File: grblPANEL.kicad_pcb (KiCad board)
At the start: 4 copper layers, 0 parts

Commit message: PCB layout - WIP
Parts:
- added C101: 470n, Capacitor_SMD:C_0805_2012Metric, F.Cu at (96.0, 131.0)
- added C102: 10u, Capacitor_SMD:C_1206_3216Metric, F.Cu at (92.0, 133.0)
- added C103: 1u, Capacitor_SMD:C_0603_1608Metric, F.Cu at (80.5, 129.0)
- added C104: 1u, Capacitor_SMD:C_0603_1608Metric, F.Cu at (78.5, 129.0)
- added C105: 10u, Capacitor_SMD:C_1206_3216Metric, F.Cu at (72.0, 129.0)
- added C106: 22u, Capacitor_SMD:C_1206_3216Metric, F.Cu at (57.5, 129.0)
- added C201: 4u7, Capacitor_SMD:C_0805_2012Metric, F.Cu at (33.5, 98.5)
- added C202: 100n, Capacitor_SMD:C_0603_1608Metric, F.Cu at (35.5, 102.0)
- added C203: 100n, Capacitor_SMD:C_0603_1608Metric, F.Cu at (35.5, 98.5)
- added C204: 100n, Capacitor_SMD:C_0603_1608Metric, F.Cu at (49.5, 102.0)
- added C205: 100n, Capacitor_SMD:C_0603_1608Metric, F.Cu at (72.0, 75.5)
- added C206: 10p, Capacitor_SMD:C_0603_1608Metric, F.Cu at (29.5, 105.5)
- added C207: 10p, Capacitor_SMD:C_0603_1608Metric, F.Cu at (35.5, 105.5)
- added C208: 100n, Capacitor_SMD:C_0603_1608Metric, F.Cu at (51.0, 97.0)
- added C301: 100n, Capacitor_SMD:C_0603_1608Metric, F.Cu at (88.5, 144.0)
- added C302: 10p, Capacitor_SMD:C_0603_1608Metric, F.Cu at (100.5, 141.0)
- added C303: 10p, Capacitor_SMD:C_0603_1608Metric, F.Cu at (100.5, 147.0)
- added C401: 100n, Capacitor_SMD:C_0603_1608Metric, F.Cu at (98.0, 157.0)
- added C501: 4u7, Capacitor_SMD:C_0805_2012Metric, F.Cu at (-30.8, 109.7)
- added C502: 100n, Capacitor_SMD:C_0603_1608Metric, F.Cu at (-42.0, 122.4)
- added C503: 100n, Capacitor_SMD:C_0603_1608Metric, F.Cu at (-50.0, 122.4)
- added C601: 10u, Capacitor_SMD:C_1206_3216Metric, F.Cu at (-69.7, 15.5)
- added C602: 100n, Capacitor_SMD:C_0603_1608Metric, F.Cu at (-76.1, 50.2)
- added D101: SMAJ24CA, Diode_SMD:D_SMA, F.Cu at (103.0, 129.0)
- added D102: D_Schottky, Diode_SMD:D_SOD-323, F.Cu at (87.5, 134.5)
- added D103: LED, LED_SMD:LED_0603_1608Metric, F.Cu at (49.0, 129.0)
- added D201: LED, LED_SMD:LED_0603_1608Metric, F.Cu at (47.0, 111.0)
- added D202: D_TVS, Diode_SMD:D_SOD-323, F.Cu at (49.5, 79.0)
- added D203: D_TVS, Diode_SMD:D_SOD-323, F.Cu at (52.0, 91.0)
- added D204: D_TVS, Diode_SMD:D_SOD-323, F.Cu at (48.0, 91.0)
- added D205: D_TVS, Diode_SMD:D_SOD-323, F.Cu at (44.0, 91.0)
- added D301: CDSOT23-SM712, Package_TO_SOT_SMD:SOT-23, F.Cu at (103.5, 144.0)
- added D401: CDSOT23-SM712, Package_TO_SOT_SMD:SOT-23, F.Cu at (104.0, 160.0)
- added D601: D_TVS, Diode_SMD:D_SOD-323, F.Cu at (-22.0, 52.0)
- added D602: D_TVS, Diode_SMD:D_SOD-323, F.Cu at (-22.0, 50.0)
- added D603: D_TVS, Diode_SMD:D_SOD-323, F.Cu at (-22.0, 48.0)
- added D604: D_TVS, Diode_SMD:D_SOD-323, F.Cu at (-22.0, 46.0)
- added D605: D_TVS, Diode_SMD:D_SOD-323, F.Cu at (-22.0, 44.0)
- added D606: D_TVS, Diode_SMD:D_SOD-323, F.Cu at (-22.0, 42.0)
- added D607: D_TVS, Diode_SMD:D_SOD-323, F.Cu at (-22.0, 40.0)
- added D608: D_TVS, Diode_SMD:D_SOD-323, F.Cu at (-22.0, 38.0)
- added D609: D_TVS, Diode_SMD:D_SOD-323, F.Cu at (-22.0, 36.0)
- added D610: D_TVS, Diode_SMD:D_SOD-323, F.Cu at (-22.0, 34.0)
- added D611: D_TVS, Diode_SMD:D_SOD-323, F.Cu at (-22.0, 32.0)
- added D612: D_TVS, Diode_SMD:D_SOD-323, F.Cu at (-22.1, 30.0)
- added D613: D_TVS, Diode_SMD:D_SOD-323, F.Cu at (-22.0, 28.0)
- added D614: D_TVS, Diode_SMD:D_SOD-323, F.Cu at (-22.0, 26.0)
- added D615: D_TVS, Diode_SMD:D_SOD-323, F.Cu at (-22.0, 24.0)
- added D616: D_TVS, Diode_SMD:D_SOD-323, F.Cu at (-22.0, 22.0)
- added D617: D_TVS, Diode_SMD:D_SOD-323, F.Cu at (-22.0, 20.0)
- added D618: D_TVS, Diode_SMD:D_SOD-323, F.Cu at (-22.0, 18.0)
- added D619: D_TVS, Diode_SMD:D_SOD-323, F.Cu at (-22.0, 16.0)
- added D701: D_TVS, Diode_SMD:D_SOD-323, F.Cu at (82.0, 176.0)
- added D702: D_TVS, Diode_SMD:D_SOD-323, F.Cu at (66.0, 176.0)
- added D703: D_TVS, Diode_SMD:D_SOD-323, F.Cu at (78.0, 176.0)
- added D704: D_TVS, Diode_SMD:D_SOD-323, F.Cu at (62.0, 176.0)
- added D705: D_TVS, Diode_SMD:D_SOD-323, F.Cu at (50.0, 176.0)
- added D706: D_TVS, Diode_SMD:D_SOD-323, F.Cu at (34.0, 176.0)
- added D707: D_TVS, Diode_SMD:D_SOD-323, F.Cu at (46.0, 176.0)
- added D708: D_TVS, Diode_SMD:D_SOD-323, F.Cu at (30.0, 176.0)
- added J101: Conn_01x02, TerminalBlock_Phoenix:TerminalBlock_Phoenix_PT-1,5-2-3.5-H_1x02_P3.50mm_Horizontal, B.Cu at (107.5, 127.2)
- added J201: 2x5x1.27mm, dresco:FTSH-105-01-L-DV-K, F.Cu at (48.0, 85.0)
- added J202: USB_C_Receptacle_USB2.0, Connector_USB:USB_C_Receptacle_HRO_TYPE-C-31-M-12, F.Cu at (64.0, 97.0)
- added J301: Conn_01x02, TerminalBlock_Phoenix:TerminalBlock_Phoenix_PT-1,5-2-3.5-H_1x02_P3.50mm_Horizontal, B.Cu at (107.5, 142.2)
- added J401: Conn_01x02, TerminalBlock_Phoenix:TerminalBlock_Phoenix_PT-1,5-2-3.5-H_1x02_P3.50mm_Horizontal, B.Cu at (107.5, 158.2)
- added J501: ILI9488, Connector_FFC-FPC:Hirose_FH12-40S-0.5SH_1x40-1MP_P0.50mm_Horizontal, F.Cu at (-46.6, 111.7)
- added J601: Conn_02x10_Odd_Even, Connector_IDC:IDC-Header_2x10_P2.54mm_Vertical, F.Cu at (-9.75, 23.1)
- added J701: Conn_01x04, TerminalBlock_Phoenix:TerminalBlock_Phoenix_PT-1,5-4-3.5-H_1x04_P3.50mm_Horizontal, B.Cu at (82.0, 179.0)
- added J702: Conn_01x04, TerminalBlock_Phoenix:TerminalBlock_Phoenix_PT-1,5-4-3.5-H_1x04_P3.50mm_Horizontal, B.Cu at (66.0, 179.0)
- added J703: Conn_01x04, TerminalBlock_Phoenix:TerminalBlock_Phoenix_PT-1,5-4-3.5-H_1x04_P3.50mm_Horizontal, B.Cu at (50.0, 179.0)
- added J704: Conn_01x04, TerminalBlock_Phoenix:TerminalBlock_Phoenix_PT-1,5-4-3.5-H_1x04_P3.50mm_Horizontal, B.Cu at (34.0, 179.0)
- added JP301: Jumper_2_Bridged, Connector_PinHeader_2.54mm:PinHeader_1x02_P2.54mm_Vertical, B.Cu at (98.2, 144.0)
- added JP401: Jumper_2_Bridged, Connector_PinHeader_2.54mm:PinHeader_1x02_P2.54mm_Vertical, B.Cu at (98.2, 160.0)
- added L101: 10n, Inductor_SMD:L_0603_1608Metric, F.Cu at (79.5, 132.0)
- added Q501: Q_NPN_BEC - S8050, Package_TO_SOT_SMD:SOT-23, F.Cu at (-57.7, 119.4)
- added R101: 2m2, Resistor_SMD:R_0603_1608Metric, F.Cu at (98.0, 131.0)
- added R102: 1m1, Resistor_SMD:R_0603_1608Metric, F.Cu at (98.0, 127.0)
- added R103: 2m2, Resistor_SMD:R_0603_1608Metric, F.Cu at (100.0, 131.0)
- added R104: 249k, Resistor_SMD:R_0603_1608Metric, F.Cu at (100.0, 127.0)
- added R105: 150k, Resistor_SMD:R_0603_1608Metric, F.Cu at (96.0, 127.0)
- added R106: 1k5, Resistor_SMD:R_0603_1608Metric, F.Cu at (87.5, 128.0)
- added R107: DNP, Resistor_SMD:R_0603_1608Metric, F.Cu at (87.5, 132.0)
- added R108: 0, Resistor_SMD:R_0603_1608Metric, F.Cu at (87.5, 130.0)
- added R109: 1k, Resistor_SMD:R_0603_1608Metric, F.Cu at (46.5, 129.0)
- added R201: 0, Resistor_SMD:R_0603_1608Metric, F.Cu at (33.5, 102.0)
- added R202: 200, Resistor_SMD:R_0603_1608Metric, F.Cu at (59.0, 75.5)
- added R203: 0, Resistor_SMD:R_0603_1608Metric, F.Cu at (52.0, 103.0)
- added R204: 0, Resistor_SMD:R_0603_1608Metric, F.Cu at (52.0, 101.0)
- added R205: 1k, Resistor_SMD:R_0603_1608Metric, F.Cu at (43.8, 111.0)
- added R206: 0, Resistor_SMD:R_0603_1608Metric, F.Cu at (32.5, 108.5)
- added R207: 5k1, Resistor_SMD:R_0603_1608Metric, F.Cu at (56.5, 100.8)
- added R208: 5k1, Resistor_SMD:R_0603_1608Metric, F.Cu at (56.5, 93.0)
- added R209: 49R9, Resistor_SMD:R_0603_1608Metric, F.Cu at (52.0, 93.0)
- added R210: 49R9, Resistor_SMD:R_0603_1608Metric, F.Cu at (48.0, 93.0)
- added R211: 49R9, Resistor_SMD:R_0603_1608Metric, F.Cu at (44.0, 93.0)
- added R301: DNP, Resistor_SMD:R_0603_1608Metric, F.Cu at (98.5, 147.0)
- added R302: 10k, Resistor_SMD:R_0603_1608Metric, F.Cu at (95.5, 140.0)
- added R303: 120, Resistor_SMD:R_0603_1608Metric, F.Cu at (98.5, 141.0)
- added R401: 10k, Resistor_SMD:R_0603_1608Metric, F.Cu at (87.0, 161.0)
- added R402: 10k, Resistor_SMD:R_0603_1608Metric, F.Cu at (87.0, 159.0)
- added R403: 120, Resistor_SMD:R_0603_1608Metric, F.Cu at (98.0, 163.0)
- added R404: DNP, Resistor_SMD:R_0603_1608Metric, F.Cu at (100.0, 163.0)
- added R405: DNP, Resistor_SMD:R_0603_1608Metric, F.Cu at (100.0, 157.0)
- added R406: 10, Resistor_SMD:R_1206_3216Metric, F.Cu at (103.5, 163.5)
- added R407: 10, Resistor_SMD:R_1206_3216Metric, F.Cu at (103.5, 156.5)
- added R501: 1k, Resistor_SMD:R_0603_1608Metric, F.Cu at (-37.1, 118.4)
- added R502: 10k, Resistor_SMD:R_0603_1608Metric, F.Cu at (-50.0, 125.0)
- added R503: 5R6, Resistor_SMD:R_0603_1608Metric, F.Cu at (-46.0, 122.4)
- added R504: 0, Resistor_SMD:R_0603_1608Metric, F.Cu at (-46.0, 125.0)
- added R505: 1k, Resistor_SMD:R_0603_1608Metric, F.Cu at (-31.0, 116.5)
- added R601: 10k, Resistor_SMD:R_0603_1608Metric, F.Cu at (-89.0, 47.0)
- added R602: 10k, Resistor_SMD:R_0603_1608Metric, F.Cu at (-61.8, 53.0)
- added R603: 10k, Resistor_SMD:R_0603_1608Metric, F.Cu at (-61.8, 55.0)
- added R604: 10k, Resistor_SMD:R_0603_1608Metric, F.Cu at (-61.8, 57.0)
- added R605: 200, Resistor_SMD:R_0603_1608Metric, F.Cu at (-29.5, 16.0)
- added R606: 200, Resistor_SMD:R_0603_1608Metric, F.Cu at (-29.5, 18.0)
- added R607: 200, Resistor_SMD:R_0603_1608Metric, F.Cu at (-29.5, 20.0)
- added R608: 200, Resistor_SMD:R_0603_1608Metric, F.Cu at (-29.5, 22.0)
- added R609: 200, Resistor_SMD:R_0603_1608Metric, F.Cu at (-29.5, 24.0)
- added R610: 200, Resistor_SMD:R_0603_1608Metric, F.Cu at (-29.5, 26.0)
- added R611: 200, Resistor_SMD:R_0603_1608Metric, F.Cu at (-29.5, 28.0)
- added R612: 200, Resistor_SMD:R_0603_1608Metric, F.Cu at (-29.5, 30.0)
- added R613: 200, Resistor_SMD:R_0603_1608Metric, F.Cu at (-29.5, 32.0)
- added R614: 200, Resistor_SMD:R_0603_1608Metric, F.Cu at (-29.5, 34.0)
- added R615: 200, Resistor_SMD:R_0603_1608Metric, F.Cu at (-29.5, 36.0)
- added R616: 200, Resistor_SMD:R_0603_1608Metric, F.Cu at (-29.5, 38.0)
- added R617: 200, Resistor_SMD:R_0603_1608Metric, F.Cu at (-29.5, 40.0)
- added R618: 200, Resistor_SMD:R_0603_1608Metric, F.Cu at (-29.5, 42.0)
- added R619: 200, Resistor_SMD:R_0603_1608Metric, F.Cu at (-29.5, 44.0)
- added R620: 200, Resistor_SMD:R_0603_1608Metric, F.Cu at (-29.5, 46.0)
- added R621: 200, Resistor_SMD:R_0603_1608Metric, F.Cu at (-29.5, 48.0)
- added R622: 200, Resistor_SMD:R_0603_1608Metric, F.Cu at (-29.5, 50.0)
- added R623: 200, Resistor_SMD:R_0603_1608Metric, F.Cu at (-29.5, 52.0)
- added R701: 200, Resistor_SMD:R_0603_1608Metric, F.Cu at (82.0, 174.0)
- added R702: 200, Resistor_SMD:R_0603_1608Metric, F.Cu at (78.0, 174.0)
- added R703: 200, Resistor_SMD:R_0603_1608Metric, F.Cu at (66.0, 174.0)
- added R704: 200, Resistor_SMD:R_0603_1608Metric, F.Cu at (62.0, 174.0)
- added R705: 200, Resistor_SMD:R_0603_1608Metric, F.Cu at (50.0, 174.0)
- added R706: 200, Resistor_SMD:R_0603_1608Metric, F.Cu at (46.0, 174.0)
- added R707: 200, Resistor_SMD:R_0603_1608Metric, F.Cu at (34.0, 174.0)
- added R708: 200, Resistor_SMD:R_0603_1608Metric, F.Cu at (30.0, 174.0)
- added SW201: SW_Push, Button_Switch_SMD:SW_Push_1P1T_NO_6x6mm_H9.5mm, F.Cu at (59.0, 69.5)
- added SW202: SW_Push, Button_Switch_SMD:SW_Push_1P1T_NO_6x6mm_H9.5mm, F.Cu at (72.0, 69.5)
- added TP101: TestPoint, TestPoint:TestPoint_THTPad_D2.0mm_Drill1.0mm, F.Cu at (103.0, 122.0)
- added TP102: TestPoint, TestPoint:TestPoint_THTPad_D2.0mm_Drill1.0mm, F.Cu at (94.0, 122.0)
- added TP103: TestPoint, TestPoint:TestPoint_THTPad_D2.0mm_Drill1.0mm, F.Cu at (90.0, 122.0)
- added TP104: TestPoint, TestPoint:TestPoint_THTPad_D2.0mm_Drill1.0mm, F.Cu at (103.0, 135.0)
- added TP105: TestPoint, TestPoint:TestPoint_THTPad_D2.0mm_Drill1.0mm, F.Cu at (65.0, 122.0)
- added TP301: TestPoint, TestPoint:TestPoint_THTPad_D2.0mm_Drill1.0mm, F.Cu at (88.5, 140.0)
- added TP302: TestPoint, TestPoint:TestPoint_THTPad_D2.0mm_Drill1.0mm, F.Cu at (88.5, 148.0)
- added TP303: TestPoint, TestPoint:TestPoint_THTPad_D2.0mm_Drill1.0mm, F.Cu at (103.0, 139.5)
- added TP304: TestPoint, TestPoint:TestPoint_THTPad_D2.0mm_Drill1.0mm, F.Cu at (103.0, 148.5)
- added TP401: TestPoint, TestPoint:TestPoint_THTPad_D2.0mm_Drill1.0mm, F.Cu at (88.5, 155.0)
- added TP402: TestPoint, TestPoint:TestPoint_THTPad_D2.0mm_Drill1.0mm, F.Cu at (88.5, 165.0)
- added TP403: TestPoint, TestPoint:TestPoint_THTPad_D2.0mm_Drill1.0mm, F.Cu at (98.5, 153.0)
- added TP404: TestPoint, TestPoint:TestPoint_THTPad_D2.0mm_Drill1.0mm, F.Cu at (102.5, 153.0)
- added TP501: TestPoint, TestPoint:TestPoint_THTPad_D2.0mm_Drill1.0mm, F.Cu at (-58.1, 123.6)
- added TP502: TestPoint, TestPoint:TestPoint_THTPad_D2.0mm_Drill1.0mm, F.Cu at (-45.1, 119.2)
- added TP503: TestPoint, TestPoint:TestPoint_THTPad_D2.0mm_Drill1.0mm, F.Cu at (-31.0, 113.2)
- added TP504: TestPoint, TestPoint:TestPoint_THTPad_D2.0mm_Drill1.0mm, F.Cu at (-53.2, 119.2)
- added TP505: TestPoint, TestPoint:TestPoint_THTPad_D2.0mm_Drill1.0mm, F.Cu at (-54.1, 123.6)
- added TP506: TestPoint, TestPoint:TestPoint_THTPad_D2.0mm_Drill1.0mm, F.Cu at (-49.2, 119.2)
- added TP507: TestPoint, TestPoint:TestPoint_THTPad_D2.0mm_Drill1.0mm, F.Cu at (-41.1, 119.2)
- added TP601: TestPoint, TestPoint:TestPoint_THTPad_D2.0mm_Drill1.0mm, F.Cu at (-58.0, 24.7)
- added TP602: TestPoint, TestPoint:TestPoint_THTPad_D2.0mm_Drill1.0mm, F.Cu at (-62.0, 24.7)
- added TP701: TestPoint, TestPoint:TestPoint_THTPad_D2.0mm_Drill1.0mm, F.Cu at (82.0, 170.0)
- added TP702: TestPoint, TestPoint:TestPoint_THTPad_D2.0mm_Drill1.0mm, F.Cu at (66.0, 170.0)
- added TP703: TestPoint, TestPoint:TestPoint_THTPad_D2.0mm_Drill1.0mm, F.Cu at (78.5, 170.0)
- added TP704: TestPoint, TestPoint:TestPoint_THTPad_D2.0mm_Drill1.0mm, F.Cu at (62.5, 170.0)
- added TP705: TestPoint, TestPoint:TestPoint_THTPad_D2.0mm_Drill1.0mm, F.Cu at (50.0, 170.0)
- added TP706: TestPoint, TestPoint:TestPoint_THTPad_D2.0mm_Drill1.0mm, F.Cu at (34.0, 170.0)
- added TP707: TestPoint, TestPoint:TestPoint_THTPad_D2.0mm_Drill1.0mm, F.Cu at (46.5, 170.0)
- added TP708: TestPoint, TestPoint:TestPoint_THTPad_D2.0mm_Drill1.0mm, F.Cu at (30.5, 170.0)
- added U101: MAX17612A, dresco:TDFN-10-1EP_3x3mm_P0.5mm_EP1.6x2.39mm_ThermalVias, F.Cu at (92.0, 129.0)
- added U102: AZ1117-3.3, Package_TO_SOT_SMD:SOT-223-3_TabPin2, F.Cu at (65.0, 129.0)
- added U201: STM32G0B1CxTxN, Package_QFP:LQFP-48_7x7mm_P0.5mm, F.Cu at (42.5, 102.0)
- added U202: USBLC6-2SC6, Package_TO_SOT_SMD:SOT-23-6, F.Cu at (55.0, 97.0)
- added U301: SN65HVD230, Package_SO:SOIC-8_3.9x4.9mm_P1.27mm, F.Cu at (93.5, 144.0)
- added U401: THVD1406, Package_SO:SOIC-8_3.9x4.9mm_P1.27mm, F.Cu at (93.0, 160.0)
- added U601: ADP5589, dresco:LFCSP-24-1EP_3.5x3.5mm_P0.4mm_EP2.2x2.2mm_ThermalVias, F.Cu at (-49.0, 30.5)
- added Y201: 8MHz, Crystal:Crystal_SMD_3225-4Pin_3.2x2.5mm, F.Cu at (32.5, 105.5)
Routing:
- net (no net): vias 0 -> 12
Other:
- board outline added: 150 x 120.5 mm
- board text added: "3.3v"
- board text added: "5-12V"
- board text added: "A"
- board text added: "B"
- board text added: "CAN H"
- board text added: "CAN L"
- board text added: "CAN TERM"
- board text added: "ENCODER 1"
- board text added: "ENCODER 2"
- board text added: "ENCODER 3"
- board text added: "ENCODER 4"
- board text added: "GND"
- board text added: "RS485 A+"
- board text added: "RS485 B-"
- board text added: "RS485 TERM"

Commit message: WIP layout
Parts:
- removed C503: 100n, Capacitor_SMD:C_0603_1608Metric
- J201, J202, J601, SW202: moved to B.Cu
- R503: value 5R6 -> 0
- R504: value 0 -> 5R6
- SW201: footprint Button_Switch_SMD:SW_Push_1P1T_NO_6x6mm_H9.5mm -> Button_Switch_SMD:SW_SPST_PTS645; moved to B.Cu
- moved TP601 218.3 mm to (138.5, 120.0)
- moved TP602 218.3 mm to (134.4, 120.0)
- moved TP506 192.3 mm to (142.5, 135.0), turned to -90 degrees
- moved TP504 190.4 mm to (136.5, 135.0), turned to -90 degrees
- moved R601 186.9 mm to (83.0, 120.0)
- moved TP505 184.9 mm to (130.5, 135.0), turned to -90 degrees
- moved TP501 184.0 mm to (125.5, 135.0), turned to -90 degrees
- moved C601 181.1 mm to (76.0, 123.0)
- moved TP503 180.8 mm to (149.5, 124.0), turned to 90 degrees
- moved TP507 171.9 mm to (130.5, 130.0), turned to -90 degrees
- moved TP502 171.0 mm to (125.5, 130.0), turned to -90 degrees
- moved C602 170.1 mm to (76.0, 126.5)
- moved R602 165.7 mm to (89.0, 121.5)
- moved R603 165.7 mm to (89.0, 123.5)
- moved R604 165.7 mm to (89.0, 125.5)
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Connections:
- net Net-(J501-Pad17) renamed /Display/DIO_GND
- J501 pad 34: Net-(J501-Pad34) -> /Display/BL_K
- J501 pad 35: Net-(J501-Pad34) -> /Display/BL_K
- J501 pad 36: Net-(J501-Pad34) -> /Display/BL_K
- R503 pad 1: Net-(Q501-Pad3) -> DISPLAY_SCL
- R503 pad 2: Net-(J501-Pad34) -> Net-(J501-Pad11)
- R504 pad 1: DISPLAY_SCL -> Net-(Q501-Pad3)
- R504 pad 2: Net-(J501-Pad11) -> /Display/BL_K
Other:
- board size 150 x 120.5 mm -> 84 x 55 mm

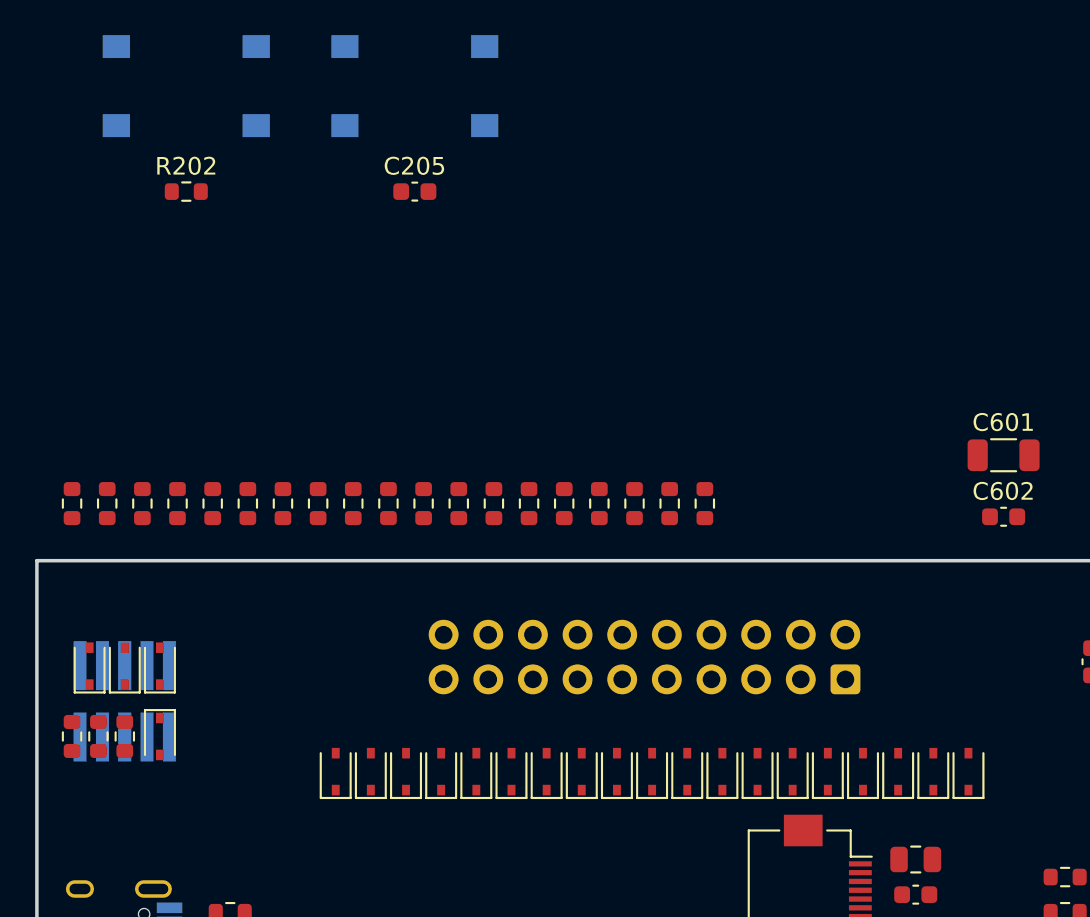
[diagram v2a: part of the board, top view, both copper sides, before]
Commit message: Resistor & TVS arrays
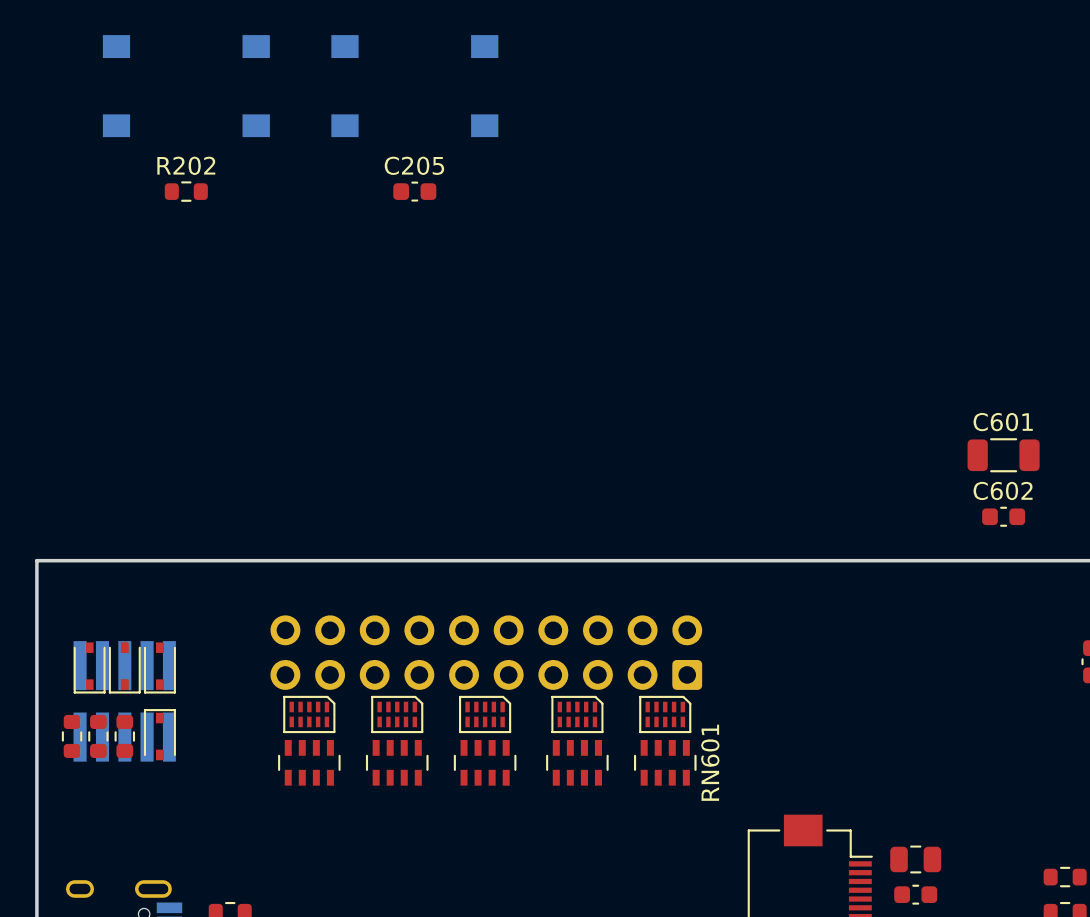
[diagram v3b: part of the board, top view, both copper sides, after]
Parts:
- removed D606, D607, D608, D609, D610, D611, D612, D613, D614, D615, D616, D617, D618, D619: D_TVS, Diode_SMD:D_SOD-323
- removed R605, R606, R607, R608, R609, R610, R611, R612, R613, R614, R615, R616, R617, R618, R619, R620, R621, R622, R623: 200, Resistor_SMD:R_0603_1608Metric
- added RN601: 200, Resistor_SMD:R_Array_Concave_4x0603, F.Cu at (56.8, 140.5)
- added RN602: 200, Resistor_SMD:R_Array_Concave_4x0603, F.Cu at (51.8, 140.5)
- added RN603: 200, Resistor_SMD:R_Array_Concave_4x0603, F.Cu at (46.5, 140.5)
- added RN604: 200, Resistor_SMD:R_Array_Concave_4x0603, F.Cu at (41.5, 140.5)
- added RN605: 200, Resistor_SMD:R_Array_Concave_4x0603, F.Cu at (36.5, 140.5)
- D601, D602, D603, D604, D605: value D_TVS -> PESD4USB3B; footprint Diode_SMD:D_SOD-323 -> dresco:SOT1176D
- SW201: footprint Button_Switch_SMD:SW_SPST_PTS645 -> Button_Switch_SMD:SW_Push_1P1T_NO_6x6mm_H9.5mm
- moved D601 19.0 mm to (56.8, 137.8), turned to 180 degrees
- moved D602 12.2 mm to (51.8, 137.8), turned to 180 degrees
- moved D605 10.0 mm to (36.5, 137.8), turned to 180 degrees
- moved J601 9.00 mm to (58.0, 135.5)
- moved D603 5.55 mm to (46.5, 137.8), turned to 180 degrees
- moved D604 4.10 mm to (41.5, 137.8), turned to 180 degrees
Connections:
- D601 pad 1: GND -> /Keypad/row0
- D601 pad 2: /Keypad/col10 -> /Keypad/row1
- D602 pad 1: GND -> /Keypad/row4
- D602 pad 2: /Keypad/col9 -> /Keypad/row5
- D603 pad 1: GND -> /Keypad/col0
- D603 pad 2: /Keypad/col8 -> /Keypad/col1
- D604 pad 1: GND -> /Keypad/col4
- D604 pad 2: /Keypad/col7 -> /Keypad/col5
- D605 pad 1: GND -> /Keypad/col8
- D605 pad 2: /Keypad/col6 -> /Keypad/col9

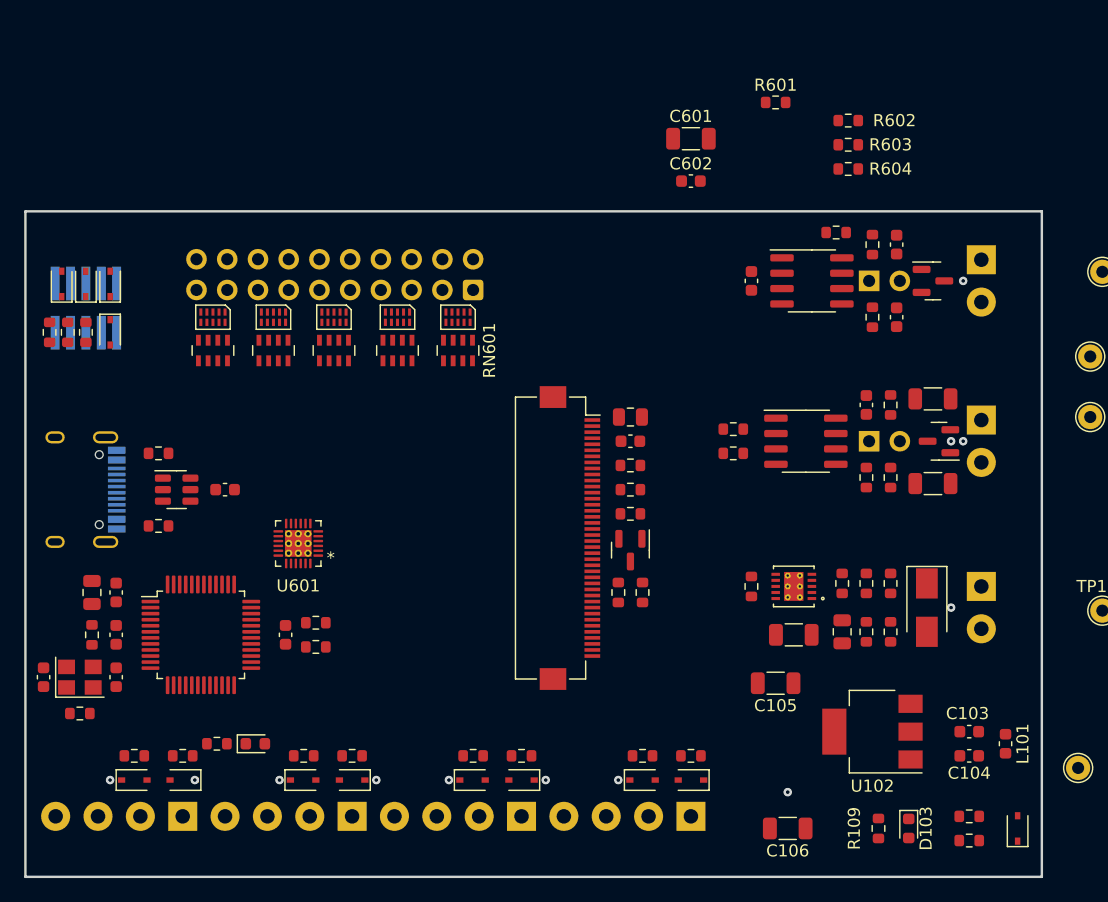
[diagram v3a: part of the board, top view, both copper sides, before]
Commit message: 1st stab at routing power input section
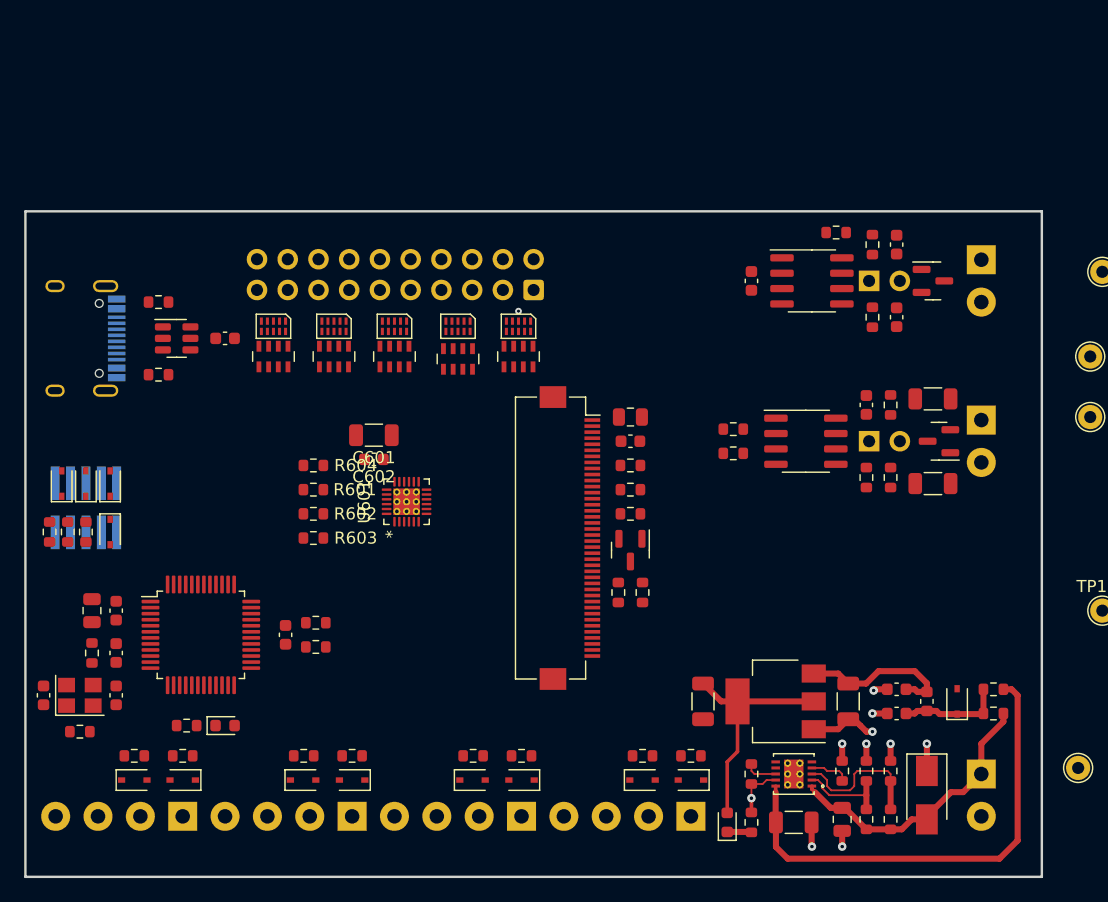
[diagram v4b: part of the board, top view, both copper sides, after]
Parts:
- moved R602 54.9 mm to (44.8, 154.0)
- moved R603 54.9 mm to (44.8, 156.0)
- moved R604 50.5 mm to (44.8, 150.0)
- moved R601 49.8 mm to (44.8, 152.0)
- moved C601 35.9 mm to (49.8, 147.5), turned to 180 degrees
- moved C602 34.9 mm to (49.8, 149.5), turned to 180 degrees
- moved D202 16.5 mm to (28.0, 155.5)
- moved D203 16.5 mm to (28.0, 151.5)
- moved D204 16.5 mm to (26.0, 151.5)
- moved D205 16.5 mm to (24.0, 151.5)
- moved J201 16.5 mm to (26.0, 153.5)
- moved R209 16.5 mm to (26.0, 155.5)
- moved R210 16.5 mm to (24.5, 155.5)
- moved R211 16.5 mm to (23.0, 155.5)
- moved C101 15.5 mm to (88.5, 179.2)
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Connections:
- RN601 pad 1: /Keypad/R0 -> /Keypad/row0
- RN601 pad 2: /Keypad/R1 -> /Keypad/row1
- RN601 pad 3: /Keypad/R2 -> /Keypad/row2
- RN601 pad 4: /Keypad/R3 -> /Keypad/row3
- RN601 pad 5: /Keypad/row3 -> /Keypad/R3
- RN601 pad 6: /Keypad/row2 -> /Keypad/R2
- RN601 pad 7: /Keypad/row1 -> /Keypad/R1
- RN601 pad 8: /Keypad/row0 -> /Keypad/R0
- RN602 pad 1: /Keypad/R4 -> /Keypad/row4
- RN602 pad 2: /Keypad/R5 -> /Keypad/row5
- RN602 pad 3: /Keypad/R6 -> /Keypad/row6
- RN602 pad 4: /Keypad/R7 -> /Keypad/row7
- RN602 pad 5: /Keypad/row7 -> /Keypad/R7
- RN602 pad 6: /Keypad/row6 -> /Keypad/R6
- RN602 pad 7: /Keypad/row5 -> /Keypad/R5
- RN602 pad 8: /Keypad/row4 -> /Keypad/R4
- RN603 pad 1: /Keypad/C0 -> /Keypad/col0
- RN603 pad 2: /Keypad/C1 -> /Keypad/col1
- RN603 pad 3: /Keypad/C2 -> /Keypad/col2
- RN603 pad 4: /Keypad/C3 -> /Keypad/col3
- RN603 pad 5: /Keypad/col3 -> /Keypad/C3
- RN603 pad 6: /Keypad/col2 -> /Keypad/C2
- RN603 pad 7: /Keypad/col1 -> /Keypad/C1
- RN603 pad 8: /Keypad/col0 -> /Keypad/C0
- RN604 pad 1: /Keypad/C4 -> /Keypad/col4
- RN604 pad 2: /Keypad/C5 -> /Keypad/col5
- RN604 pad 3: /Keypad/C6 -> /Keypad/col6
- RN604 pad 4: /Keypad/C7 -> /Keypad/col7
- RN604 pad 5: /Keypad/col7 -> /Keypad/C7
- RN604 pad 6: /Keypad/col6 -> /Keypad/C6
- RN604 pad 7: /Keypad/col5 -> /Keypad/C5
- RN604 pad 8: /Keypad/col4 -> /Keypad/C4
- RN605 pad 1: /Keypad/C8 -> /Keypad/col8
- RN605 pad 2: /Keypad/C9 -> /Keypad/col9
- RN605 pad 3: /Keypad/C10 -> /Keypad/col10
- RN605 pad 6: /Keypad/col10 -> /Keypad/C10
- RN605 pad 7: /Keypad/col9 -> /Keypad/C9
- RN605 pad 8: /Keypad/col8 -> /Keypad/C8
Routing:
- net /Power/VIN_PROT: track 0.00 -> 39.4 mm
- net VIN: track 0.00 -> 23.0 mm
- net GND: track 0.00 -> 21.9 mm, vias 0 -> 11
- net +3V3: track 0.00 -> 19.3 mm
- net /Power/VIN_PI_OUT: track 0.00 -> 13.1 mm
- net /Power/OVLO: track 0.00 -> 11.6 mm
- net /Power/VIN_PI_IN: track 0.00 -> 8.55 mm
- net /Power/ULVO: track 0.00 -> 7.56 mm
- net /Power/CLMODE: track 0.00 -> 3.29 mm
- net /Power/SETI: track 0.00 -> 2.68 mm
- net /Power/PWR_LED_K: track 0.00 -> 2.02 mm
- net (no net): vias 12 -> 0
- added copper zone on In1.Cu, net GND
- added copper zone on In2.Cu, net GND
